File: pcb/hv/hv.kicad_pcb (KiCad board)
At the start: 2 copper layers, 85 x 40 mm, 40 parts, among them Q1 IRL540N, Q151 TN2106N3-G, T1 DA2032-AL, U5 LM5155

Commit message: Rev B RC1
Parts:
- added J1: JST XH, Connector_JST:JST_XH_S6B-XH-A_1x06_P2.50mm_Horizontal, F.Cu at (120.0, 120.0)
- added J2: Phoenix MSTB, Connector_Phoenix_MSTB:PhoenixContact_MSTBA_2,5_3-G-5,08_1x03_P5.08mm_Horizontal, F.Cu at (164.8, 120.0)
- moved H2 15.0 mm to (110.0, 125.0)
- moved H4 15.0 mm to (185.0, 125.0)
- moved TP2 7.38 mm to (173.0, 81.0)
- moved TP1 1.64 mm to (181.0, 90.0)
- moved RV1 0.10 mm to (126.9, 106.6)
- renumbered C5 to C1, C12 to C10, C10 to C11, C6 to C2, C13 to C3, C14 to C4, C15 to C5, C109 to C6, C11 to C7, C7 to C8, D3 to D1, D1 to D3, H6 to H1, H8 to H2, H7 to H3, H9 to H4, Q151 to Q2, R12 to R1, R7 to R10, R16 to R11, R18 to R12, R19 to R13, R10 to R14, R11 to R15, R20 to R2, R160 to R3, R13 to R4, R8 to R5, R14 to R6, R9 to R7, R17 to R8, R15 to R9, TP2 to TP1, TP1 to TP2, U5 to U1
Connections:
- net /HV/COMP renamed /COMP
- net /HV/CS renamed /CS
- net /HV/FB renamed /FB
- net /HV/GATE_{IRL540N} renamed /GATE_{IRL540N}
- net /HV/GATE_{LM5155} renamed /GATE_{LM5155}
- net /HV/HV_{DIV} renamed /HV_{DIV}
- net /HV/HV_{SEC} renamed /HV_{SEC}
- net /HV/RT renamed /RT
- net /HV/SOURCE_{IRL540N} renamed /SOURCE_{IRL540N}
- net /HV/SS renamed /SS
- net /HV/UVLO renamed /UVLO
- net /HV/VCC renamed /VCC
- net /HV/V_{SW} renamed /V_{SW}
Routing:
- net +170V: track 36.2 -> 71.2 mm
- net EN_{HV}: track 4.58 -> 37.6 mm
- net PGOOD_{LM5155}: track 14.4 -> 44.6 mm
- net V_{BUS}: track 71.7 -> 85.6 mm
- net +3V3: track 5.78 -> 19.2 mm
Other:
- board size 85 x 40 mm -> 85 x 55 mm
- board text added: "${TITLE}//REV ${REV}//${AUTHOR}"

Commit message: Final Rev B
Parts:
- added REF**: Symbol_HighVoltage_Triangle_8x7mm_SilkScreen, nixie_clock:Symbol_HighVoltage_Triangle_8x7mm_SilkScreen, F.Cu at (155.0, 120.0)
- added REF**: Symbol_HighVoltage_Triangle_8x7mm_SilkScreen, nixie_clock:Symbol_HighVoltage_Triangle_8x7mm_SilkScreen, B.Cu at (155.0, 120.0)
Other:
- board text removed: "170V Supply"

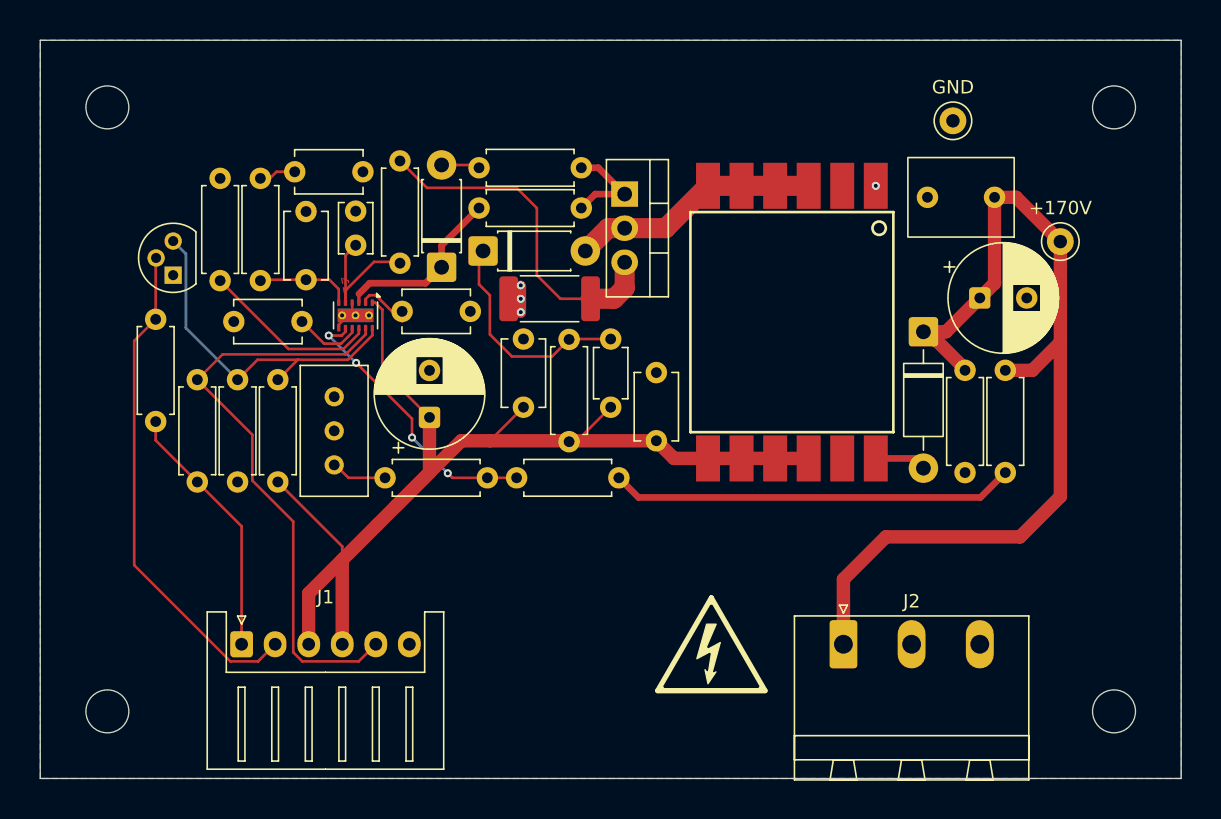
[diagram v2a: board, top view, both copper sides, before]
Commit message: HV converter Rev C redesign around LM5156
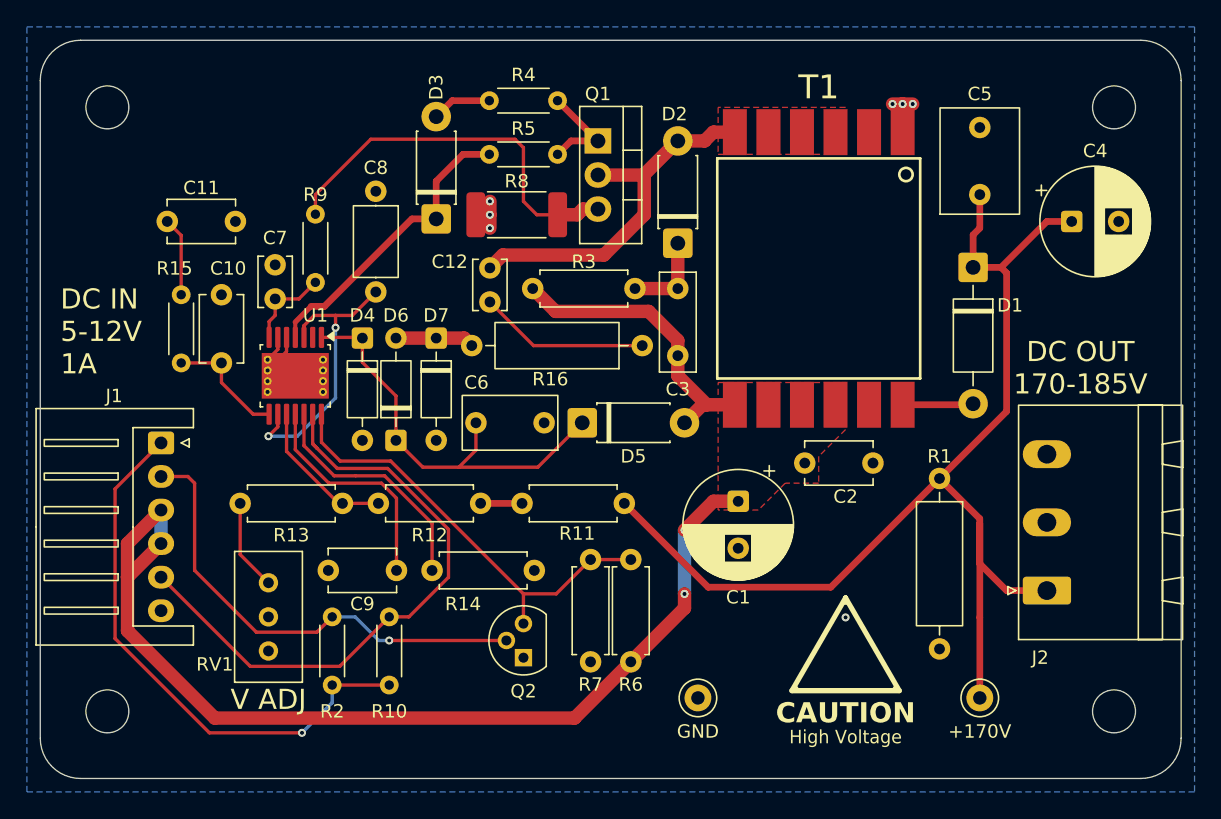
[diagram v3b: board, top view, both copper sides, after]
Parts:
- removed the REF** at (155.0, 120.0) (x2)
- added C12: 4.7nF, C0G, 0_nixie_clock:C_Rect_L3.8mm_W2.5mm_P2.54mm_Goldmax, F.Cu at (138.5, 93.2)
- added D4: ZPD3B0, Diode_THT:D_DO-35_SOD27_P7.62mm_Horizontal, F.Cu at (129.0, 97.2)
- added D5: SB140-T, Diode_THT:D_DO-41_SOD81_P7.62mm_Horizontal, F.Cu at (145.4, 103.5)
- added D6: 1N4148, Diode_THT:D_DO-35_SOD27_P7.62mm_Horizontal, F.Cu at (131.5, 104.8)
- added D7: 1N4148, Diode_THT:D_DO-35_SOD27_P7.62mm_Horizontal, F.Cu at (134.5, 97.2)
- added R16: 82, Resistor_THT:R_Axial_DIN0309_L9.0mm_D3.2mm_P12.70mm_Horizontal, F.Cu at (149.8, 97.8)
- added REF**: Symbol_HighVoltage_Triangle_8x7mm_CopperArrow, 0_nixie_clock:Symbol_HighVoltage_Triangle_8x7mm_CopperArrow, F.Cu at (165.0, 120.0)
- C1, C4: footprint Capacitor_THT:CP_Radial_D8.0mm_P3.50mm -> 0_nixie_clock:CP_Radial_D8.0mm_P3.50mm
- C10: value 220pF -> 220pF, C0G; footprint nixie_clock:C_Rect_L5.1mm_W3.2mm_P5.08mm_Goldmax -> 0_nixie_clock:C_Rect_L5.1mm_W3.2mm_P5.08mm_Goldmax
- C11, C2: footprint nixie_clock:C_Rect_L5.1mm_W3.2mm_P5.08mm_Goldmax -> 0_nixie_clock:C_Rect_L5.1mm_W3.2mm_P5.08mm_Goldmax
- C3: footprint nixie_clock:C_Rect_L3.8mm_W2.5mm_P5.08mm_Goldmax -> 0_nixie_clock:C_Rect_L7.2mm_W2.5mm_P5.00mm_PHE426
- C5: footprint nixie_clock:C_Rect_L7.9mm_W5.9mm_P5.00mm_ECQE -> 0_nixie_clock:C_Rect_L7.9mm_W5.9mm_P5.00mm_ECQE
- C6: value 10nF -> 1uF; footprint nixie_clock:C_Rect_L5.1mm_W3.2mm_P5.08mm_Goldmax -> 0_nixie_clock:C_Rect_L7.1mm_W4.1mm_P5.08mm_Goldmax
- C7: value 470pF -> 470pF, C0G; footprint nixie_clock:C_Rect_L3.8mm_W2.5mm_P2.54mm_Goldmax -> 0_nixie_clock:C_Rect_L3.8mm_W2.5mm_P2.54mm_Goldmax
- C8: footprint nixie_clock:C_Rect_L5.1mm_W3.2mm_P5.08mm_Goldmax -> Capacitor_THT:C_Axial_L5.1mm_D3.1mm_P7.50mm_Horizontal
- C9: value 220nF -> 470nF; footprint nixie_clock:C_Rect_L5.1mm_W3.2mm_P5.08mm_Goldmax -> 0_nixie_clock:C_Rect_L5.1mm_W3.2mm_P5.08mm_Goldmax
- R1: renamed from R2; footprint Resistor_THT:R_Axial_DIN0207_L6.3mm_D2.5mm_P7.62mm_Horizontal -> Resistor_THT:R_Axial_DIN0309_L9.0mm_D3.2mm_P12.70mm_Horizontal
- R10, R15, R4, R9: footprint Resistor_THT:R_Axial_DIN0207_L6.3mm_D2.5mm_P7.62mm_Horizontal -> Resistor_THT:R_Axial_DIN0204_L3.6mm_D1.6mm_P5.08mm_Horizontal
- R11: renamed from R8; value 866k -> 845k
- R12: value 866k -> 845k
- R13: value 8.87k -> 8.25k
- R2: renamed from R3; footprint Resistor_THT:R_Axial_DIN0207_L6.3mm_D2.5mm_P7.62mm_Horizontal -> Resistor_THT:R_Axial_DIN0204_L3.6mm_D1.6mm_P5.08mm_Horizontal
- R5: renamed from R6; footprint Resistor_THT:R_Axial_DIN0207_L6.3mm_D2.5mm_P7.62mm_Horizontal -> Resistor_THT:R_Axial_DIN0204_L3.6mm_D1.6mm_P5.08mm_Horizontal
- R6: renamed from R5; value 143k -> 63.4k
- T1: footprint nixie_clock:DA2032-AL -> 0_nixie_clock:DA2032-AL
- U1: value LM5155 -> LM5156H; footprint nixie_clock:WSON-12-1EP_3x2mm_P0.5mm_EP1x2.65_ThermalVias -> 0_nixie_clock:Texas_HTSSOP-14-1EP_4.4x5mm_P0.65mm_EP3.4x5mm_Mask3.155x3.255mm_ThermalVias
- moved TP2 47.0 mm to (154.0, 124.0)
- moved Q2 38.6 mm to (141.0, 121.0)
- moved TP1 34.5 mm to (175.0, 124.0)
- moved R11 30.1 mm to (148.5, 109.5), turned to 180 degrees
- moved R6 29.5 mm to (149.0, 121.3)
- moved R7 29.5 mm to (146.0, 113.7)
- moved R14 26.7 mm to (134.2, 114.5), turned to 0 degrees
- moved C1 23.8 mm to (157.0, 109.3), turned to -90 degrees
- moved R2 23.6 mm to (126.8, 123.0)
- moved R10 20.8 mm to (131.0, 123.0)
- moved C9 19.8 mm to (129.0, 114.5)
- moved J1 16.2 mm to (114.0, 105.0), turned to -90 degrees
- moved J2 15.7 mm to (180.0, 116.0), turned to 90 degrees
- moved D2 14.5 mm to (152.5, 90.1), turned to 90 degrees
- moved C2 14.2 mm to (164.5, 106.5), turned to 0 degrees
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- renumbered R1 to R3, R11 to R8
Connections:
- net /GATE_{IRL540N} renamed /GATE_{2}
- net /SOURCE_{IRL540N} renamed /SOURCE_{SW}
- net EN_{HV} renamed ~{EN}_{HV}
- net Net-(D2-K) renamed /SW_{CLAMP}
- C6 pad 2: V_{BUS} -> /BIAS
- D3 pad 1: /GATE_{LM5155} -> /GATE_{1}
- J1 pad 5: PGOOD_{LM5155} -> PGOOD_{HV}
- R10 pad 2: PGOOD_{LM5155} -> PGOOD_{HV}
- R5 pad 1: /GATE_{LM5155} -> /GATE_{1}
- U1 pad 1: V_{BUS} -> /BIAS
- U1 pad 10: /RT -> /FB
- U1 pad 11: PGOOD_{LM5155} -> /SS
- U1 pad 12: /UVLO -> /RT
- U1 pad 13: GND -> PGOOD_{HV}
- U1 pad 2: /VCC -> unconnected-(U1-NC-Pad2)
- U1 pad 3: /GATE_{LM5155} -> /VCC
- U1 pad 4: GND -> /GATE_{1}
- U1 pad 5: /CS -> GND
- U1 pad 6: /COMP -> GND
- U1 pad 7: GND -> /CS
- U1 pad 8: /FB -> /COMP
- U1 pad 9: /SS -> /VCC
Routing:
- net PGOOD_{HV}: track 0.00 -> 45.8 mm
- net PGOOD_{LM5155}: track 44.6 -> 0.00 mm
- net /BIAS: track 0.00 -> 31.6 mm
- net /HV_{DIV}: track 30.2 -> 3.09 mm
- net /GATE_{1}: track 0.00 -> 22.4 mm
- net +3V3: track 19.2 -> 41.6 mm, vias 0 -> 1
- net /VCC: track 3.92 -> 21.5 mm, vias 0 -> 2
- net +170V: track 71.2 -> 88.2 mm
- net /GATE_{LM5155}: track 13.2 -> 0.00 mm
- net Net-(C12-Pad2): track 0.00 -> 12.7 mm
- net /SS: track 5.09 -> 17.1 mm
- net V_{BUS}: track 85.6 -> 97.1 mm, vias 0 -> 2
- net /SW_{CLAMP}: track 16.5 -> 6.57 mm
- net /FB: track 20.8 -> 11.2 mm, vias 4 -> 0
- net /V_{SW}: track 18.7 -> 27.6 mm
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- added copper zone on F.Cu, net /V_{SW}
- added copper zone on F.Cu, net GND
- added copper zone on F.Cu, net V_{BUS}
- removed copper zone on F.Cu, net /GATE_{LM5155}
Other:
- outline, holes or cut-outs redrawn
- board text added: "${TITLE}//REV ${REV}//${AUTHOR} jason@ak6te.com"
- board text added: "3.3V"
- board text added: "DC IN 5-12V 1A"
- board text added: "DC OUT 170-185V"
- board text added: "GND"
- board text added: "Inhibit"
- board text added: "NC"
- board text added: "PGOOD"
- board text added: "V ADJ"
- board text added: "VIN"
- board text added: "VOUT"
- board text removed: "${TITLE}//REV ${REV}//${AUTHOR}"

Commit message: Update release process, update analysis to use INS-1 throughout
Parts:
- T1: value DA2032-AL -> >VALUE

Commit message: Update fab attributes, update silscreen to include step
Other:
- board text added: "${TITLE}//REV ${REV}${STEP}//${AUTHOR} jason@ak6te.com"
- board text removed: "${TITLE}//REV ${REV}//${AUTHOR} jason@ak6te.com"
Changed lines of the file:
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@@
 		(sheetname "/")
 		(sheetfile "hv.kicad_sch")
+		(attr through_hole)
 		(duplicate_pad_numbers_are_jumpers no)
 		(fp_rect
@@
 		(sheetname "/")
 		(sheetfile "hv.kicad_sch")
+		(attr through_hole)
 		(duplicate_pad_numbers_are_jumpers no)
 		(fp_line
@@
 		(sheetname "/")
 		(sheetfile "hv.kicad_sch")
+		(attr through_hole)
 		(duplicate_pad_numbers_are_jumpers no)
 		(fp_line
@@
 		(sheetname "/")
 		(sheetfile "hv.kicad_sch")
+		(attr through_hole)
 		(duplicate_pad_numbers_are_jumpers no)
 		(fp_line
@@
 		(sheetname "/")
 		(sheetfile "hv.kicad_sch")
+		(attr through_hole)
 		(duplicate_pad_numbers_are_jumpers no)
 		(fp_rect
@@
 		(sheetname "/")
 		(sheetfile "hv.kicad_sch")
+		(attr through_hole)
 		(duplicate_pad_numbers_are_jumpers no)
 		(fp_line
@@
 		)
 	)
-	(gr_text "${TITLE}//REV ${REV}//${AUTHOR}\njason@ak6te.com"
+	(gr_text "${TITLE}//REV ${REV}${STEP}//${AUTHOR}\njason@ak6te.com"
 		(at 162 98 0)
 		(layer "B.SilkS")
